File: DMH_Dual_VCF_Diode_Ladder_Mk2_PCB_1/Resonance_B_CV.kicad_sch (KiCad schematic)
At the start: 24 parts, among them Q3 BC548, Q4 BC548, U2 TL074

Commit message: Added board-to-board pins to schematic
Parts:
- added J18: Conn_01x10_PinHeader, Connector_PinHeader_2.54mm:PinHeader_1x10_P2.54mm_Vertical, symbol SynthStuff:Conn_01x10_PinHeader
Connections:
- net GND: now also J18.10 (Pin_10)
- net Res CV Input: now also J18.7 (Pin_7)
- net at RV20.2, U2.3 (+): now also J18.8 (Pin_8)
- net at R82.1, RV22.2: now also J18.9 (Pin_9)

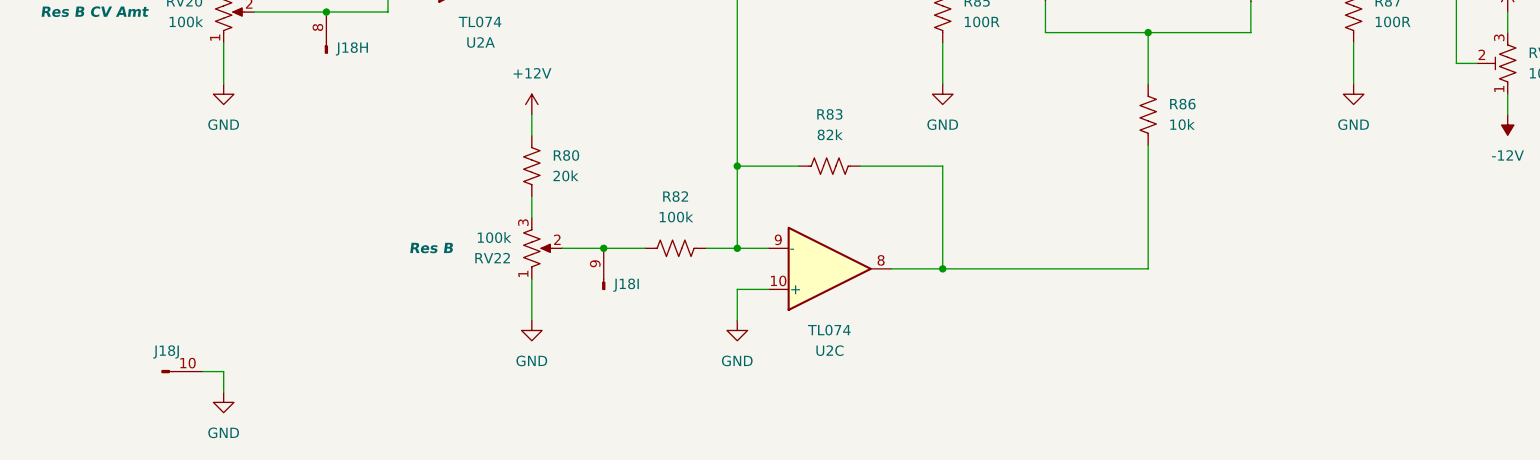
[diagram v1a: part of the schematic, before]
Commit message: Created Drive CV circuits
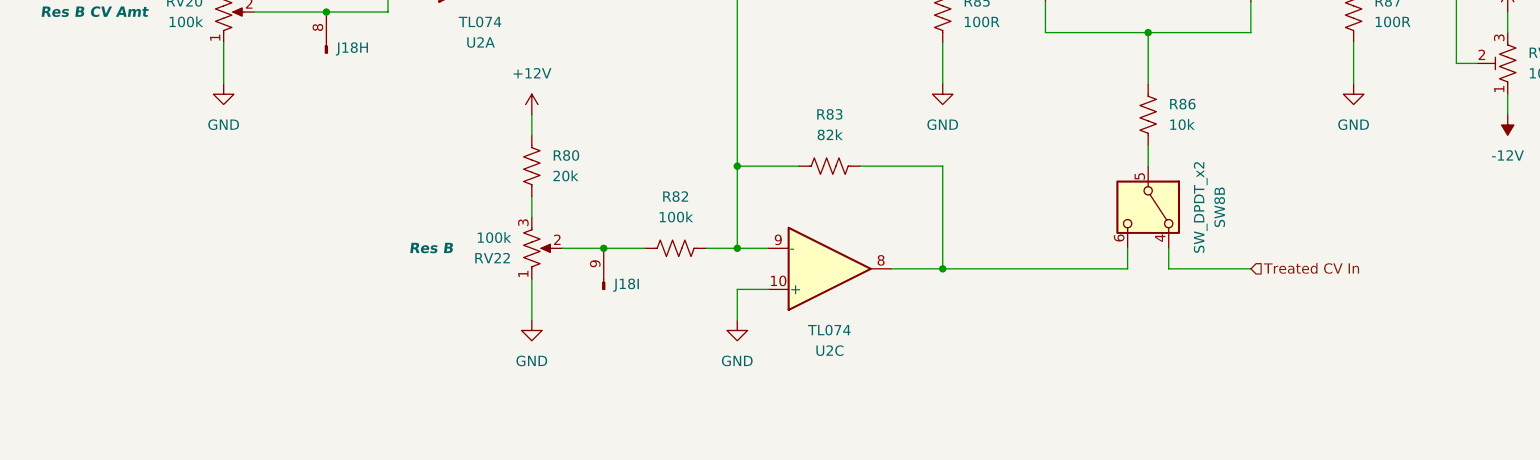
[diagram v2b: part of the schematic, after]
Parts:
- removed unit 10 of J18
- added SW8: SW_DPDT_x2, SynthStuff:Toggle_Switch_2_Poles_TE, symbol Switch:SW_DPDT_x2
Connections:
- net at R83.2, U2.8: now also SW8.6 (C); no longer R86.1
- new net: R86.1, SW8.5 (B)
- new net Treated CV In: SW8.4 (A)
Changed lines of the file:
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@@
 	)
 	(junction
-		(at 152.4 127)
+		(at 127 124.46)
 		(diameter 0)
 		(color 0 0 0 0)
 	)
 	(junction
-		(at 127 124.46)
+		(at 152.4 127)
 		(diameter 0)
 		(color 0 0 0 0)
@@
 	(wire
 		(pts
-			(xy 60.96 139.7) (xy 63.5 139.7)
-		)
-		(stroke
-			(width 0)
-			(type default)
-		)
-	)
-	(wire
-		(pts
 			(xy 215.9 88.9) (xy 215.9 101.6)
 		)
@@
 	(wire
 		(pts
+			(xy 152.4 127) (xy 175.26 127)
+		)
+		(stroke
+			(width 0)
+			(type default)
+		)
+	)
+	(wire
+		(pts
 			(xy 165.1 35.56) (xy 165.1 44.45)
 		)
@@
 	(wire
 		(pts
-			(xy 152.4 127) (xy 177.8 127)
+			(xy 180.34 127) (xy 190.5 127)
 		)
 		(stroke
@@
 	(wire
 		(pts
+			(xy 175.26 124.46) (xy 175.26 127)
+		)
+		(stroke
+			(width 0)
+			(type default)
+		)
+	)
+	(wire
+		(pts
 			(xy 198.12 88.9) (xy 203.2 88.9)
 		)
@@
 	(wire
 		(pts
+			(xy 177.8 111.76) (xy 177.8 114.3)
+		)
+		(stroke
+			(width 0)
+			(type default)
+		)
+	)
+	(wire
+		(pts
 			(xy 215.9 53.34) (xy 222.25 53.34)
 		)
@@
 	(wire
 		(pts
+			(xy 180.34 124.46) (xy 180.34 127)
+		)
+		(stroke
+			(width 0)
+			(type default)
+		)
+	)
+	(wire
+		(pts
 			(xy 177.8 97.79) (xy 177.8 104.14)
 		)
@@
 	(wire
 		(pts
-			(xy 63.5 142.24) (xy 63.5 139.7)
-		)
-		(stroke
-			(width 0)
-			(type default)
-		)
-	)
-	(wire
-		(pts
-			(xy 177.8 127) (xy 177.8 111.76)
-		)
-		(stroke
-			(width 0)
-			(type default)
-		)
-	)
-	(wire
-		(pts
 			(xy 63.5 99.06) (xy 63.5 104.14)
 		)
@@
 		)
 	)
+	(hierarchical_label "Treated CV In"
+		(shape input)
+		(at 190.5 127 0)
+		(fields_autoplaced yes)
+		(effects
+			(font
+				(size 1.27 1.27)
+			)
+			(justify left)
+		)
+	)
 	(hierarchical_label "Output"
 		(shape output)
@@
 	)
 	(symbol
-		(lib_id "SynthStuff:Conn_01x10_PinHeader")
-		(at 55.88 139.7 0)
-		(unit 10)
+		(lib_id "Switch:SW_DPDT_x2")
+		(at 177.8 119.38 270)
+		(unit 2)
 		(exclude_from_sim no)
 		(in_bom yes)
 		(on_board yes)
 		(dnp no)
-		(fields_autoplaced yes)
-		(property "Reference" "J18"
-			(at 56.515 137.16 0)
+		(property "Reference" "SW8"
+			(at 186.69 119.38 0)
 			(effects
 				(font
@@
 			)
 		)
-		(property "Value" "Conn_01x10_PinHeader"
-			(at 55.88 142.24 0)
+		(property "Value" "SW_DPDT_x2"
+			(at 184.15 119.38 0)
 			(effects
 				(font
 					(size 1.27 1.27)
 				)
-				(hide yes)
 			)
 		)
-		(property "Footprint" "Connector_PinHeader_2.54mm:PinHeader_1x10_P2.54mm_Vertical"
-			(at 55.88 139.7 0)
+		(property "Footprint" "SynthStuff:Toggle_Switch_2_Poles_TE"
+			(at 177.8 119.38 0)
 			(effects
 				(font
@@
 		)
 		(property "Datasheet" "~"
-			(at 55.88 139.7 0)
+			(at 177.8 119.38 0)
 			(effects
 				(font
@@
 			)
 		)
-		(property "Description" "Generic connector, single row, 01x10"
-			(at 55.88 139.7 0)
+		(property "Description" "Switch, dual pole double throw, separate symbols"
+			(at 177.8 119.38 0)
 			(effects
 				(font
@@
 			)
 		)
+		(pin "6"
+		)
 		(pin "5"
 		)
 		(pin "3"
 		)
-		(pin "7"
-		)
 		(pin "1"
 		)
-		(pin "9"
-		)
 		(pin "4"
 		)
 		(pin "2"
 		)
-		(pin "10"
-		)
-		(pin "6"
-		)
-		(pin "8"
-		)
 		(instances
 			(project ""
 				(path "/58f4306d-5387-4983-bb08-41a2313fd315/f0045393-e1d0-4de8-baba-b9053cd8a11d"
-					(reference "J18")
-					(unit 10)
+					(reference "SW8")
+					(unit 2)
 				)
 			)
@@
 					(unit 1)
 				)
-			)
-		)
-	)
-	(symbol
-		(lib_id "power:GND")
-		(at 63.5 142.24 0)
-		(unit 1)
-		(exclude_from_sim no)
-		(in_bom yes)
-		(on_board yes)
-		(dnp no)
-		(fields_autoplaced yes)
-		(property "Reference" "#PWR079"
-			(at 63.5 148.59 0)
-			(effects
-				(font
-					(size 1.27 1.27)
-				)
-				(hide yes)
-			)
-		)
-		(property "Value" "GND"
-			(at 63.5 147.32 0)
-			(effects
-				(font
-					(size 1.27 1.27)
-				)
-			)
-		)
-		(property "Footprint" ""
-			(at 63.5 142.24 0)
-			(effects
-				(font
-					(size 1.27 1.27)
-				)
-				(hide yes)
-			)
-		)
-		(property "Datasheet" ""
-			(at 63.5 142.24 0)
-			(effects
-				(font
-					(size 1.27 1.27)
-				)
-				(hide yes)
-			)
-		)
-		(property "Description" "Power symbol creates a global label with name \"GND\" , ground"
-			(at 63.5 142.24 0)
-			(effects
-				(font
-					(size 1.27 1.27)
-				)
-				(hide yes)
-			)
-		)
-		(pin "1"
-		)
-		(instances
-			(project "DMH_Dual_VCF_Diode_Ladder_Mk2_PCB_1"
-				(path "/58f4306d-5387-4983-bb08-41a2313fd315/f0045393-e1d0-4de8-baba-b9053cd8a11d"
-					(reference "#PWR079")
-					(unit 1)
-				)

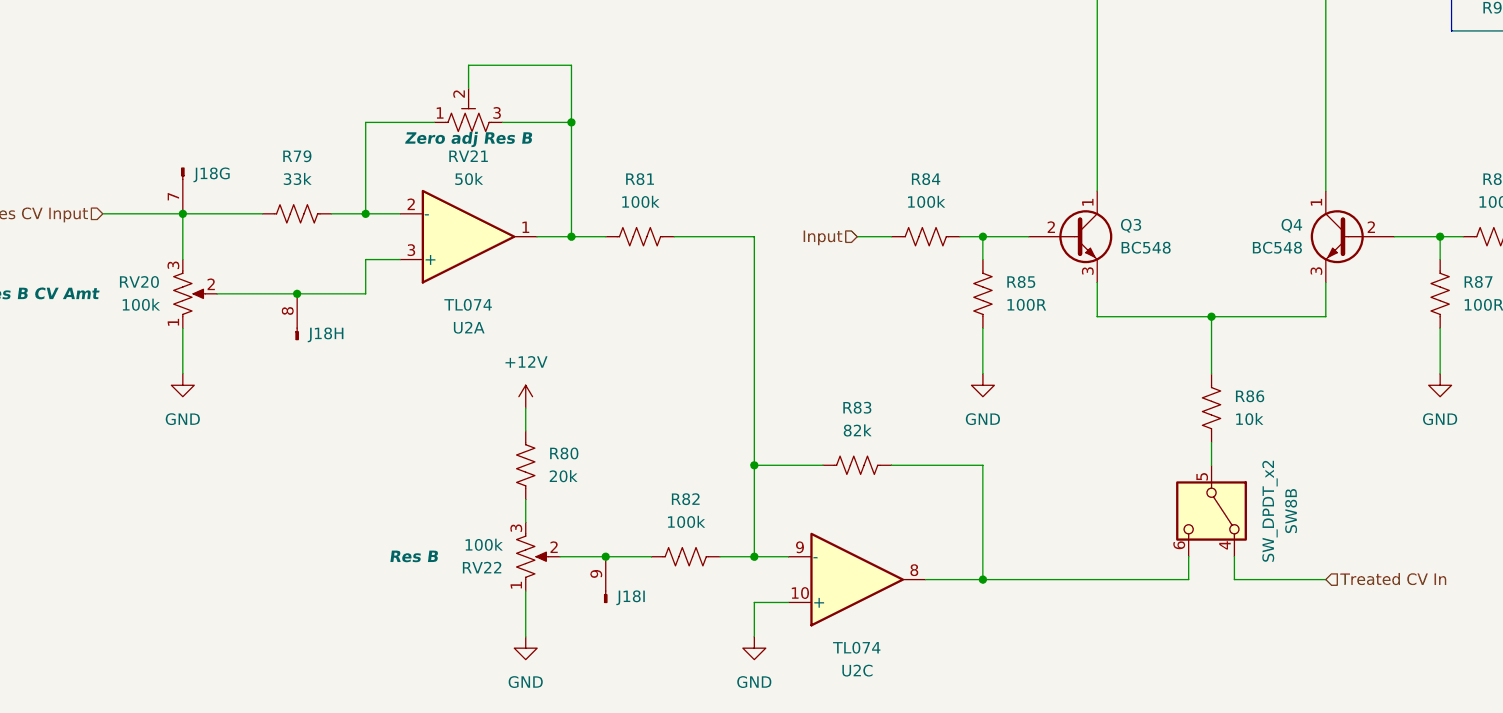
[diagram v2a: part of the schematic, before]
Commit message: Added inter-board pins to all circuits
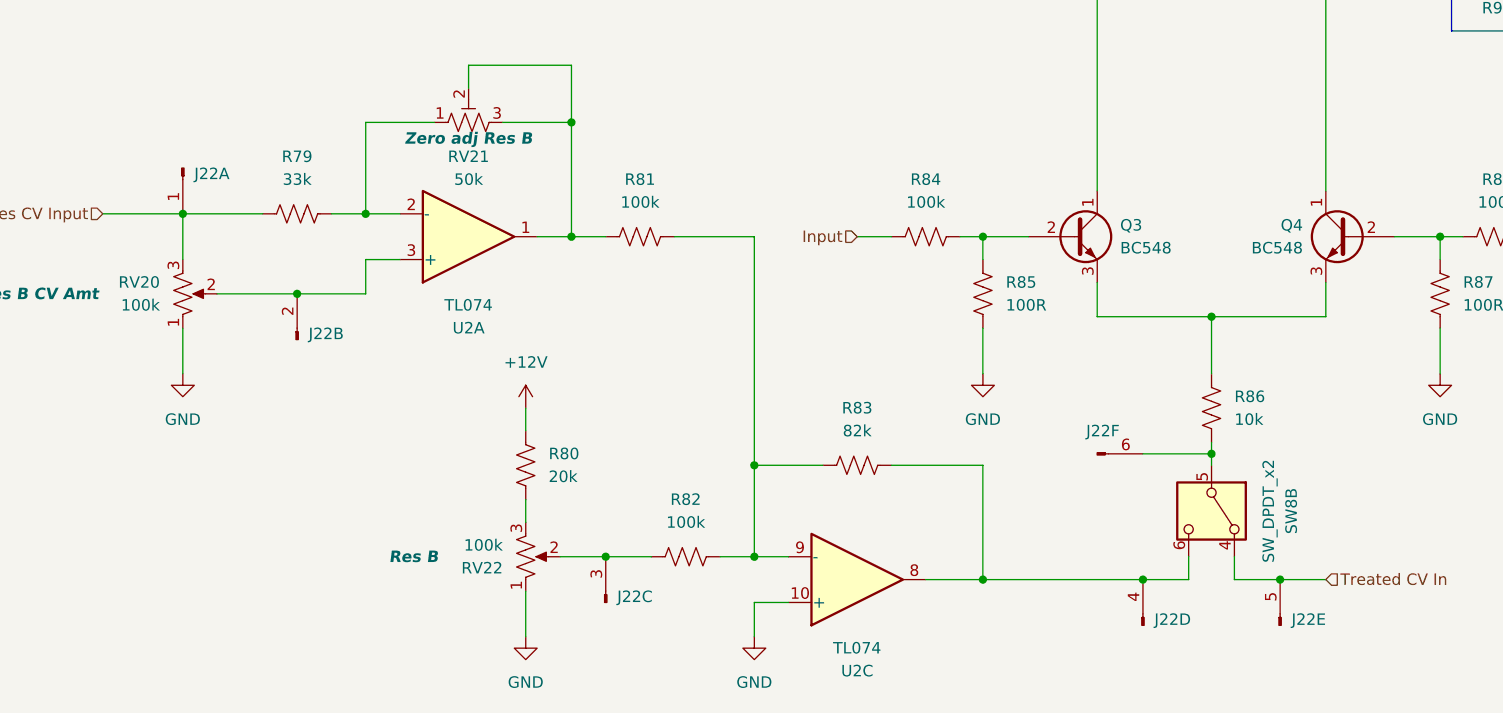
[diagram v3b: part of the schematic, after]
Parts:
- added unit 4 of J22
- added unit 6 of J22
- added unit 5 of J22
- J22: renamed from J18; value Conn_01x10_PinHeader -> Conn_01x06_PinHeader; symbol SynthStuff:Conn_01x10_PinHeader -> SynthStuff:Conn_01x06_PinHeader
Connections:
- net Res CV Input: now also J22.1 (Pin_1); no longer J22.7 (Pin_7)
- net Treated CV In: now also J22.5 (Pin_5)
- net at RV20.2, U2.3 (+): now also J22.2 (Pin_2); no longer J22.8 (Pin_8)
- net at R86.1, SW8.5 (B): now also J22.6 (Pin_6)
- net at R83.2, SW8.6 (C), U2.8: now also J22.4 (Pin_4)
- net at R82.1, RV22.2: now also J22.3 (Pin_3); no longer J22.9 (Pin_9)
